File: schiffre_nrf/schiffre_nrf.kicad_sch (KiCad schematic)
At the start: 30 parts, among them J1 Conn_01x02, J2 Conn_01x04, J3 Conn_01x01_Pin, J4 Conn_01x04, J5 FH34SRJ-30S-0.5SH(50), P1 USB_C_Plug_USB2.0, Q1 AO3407, Q2 AO3407, U1 E73-2G4M08S1C, U2 XC6220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

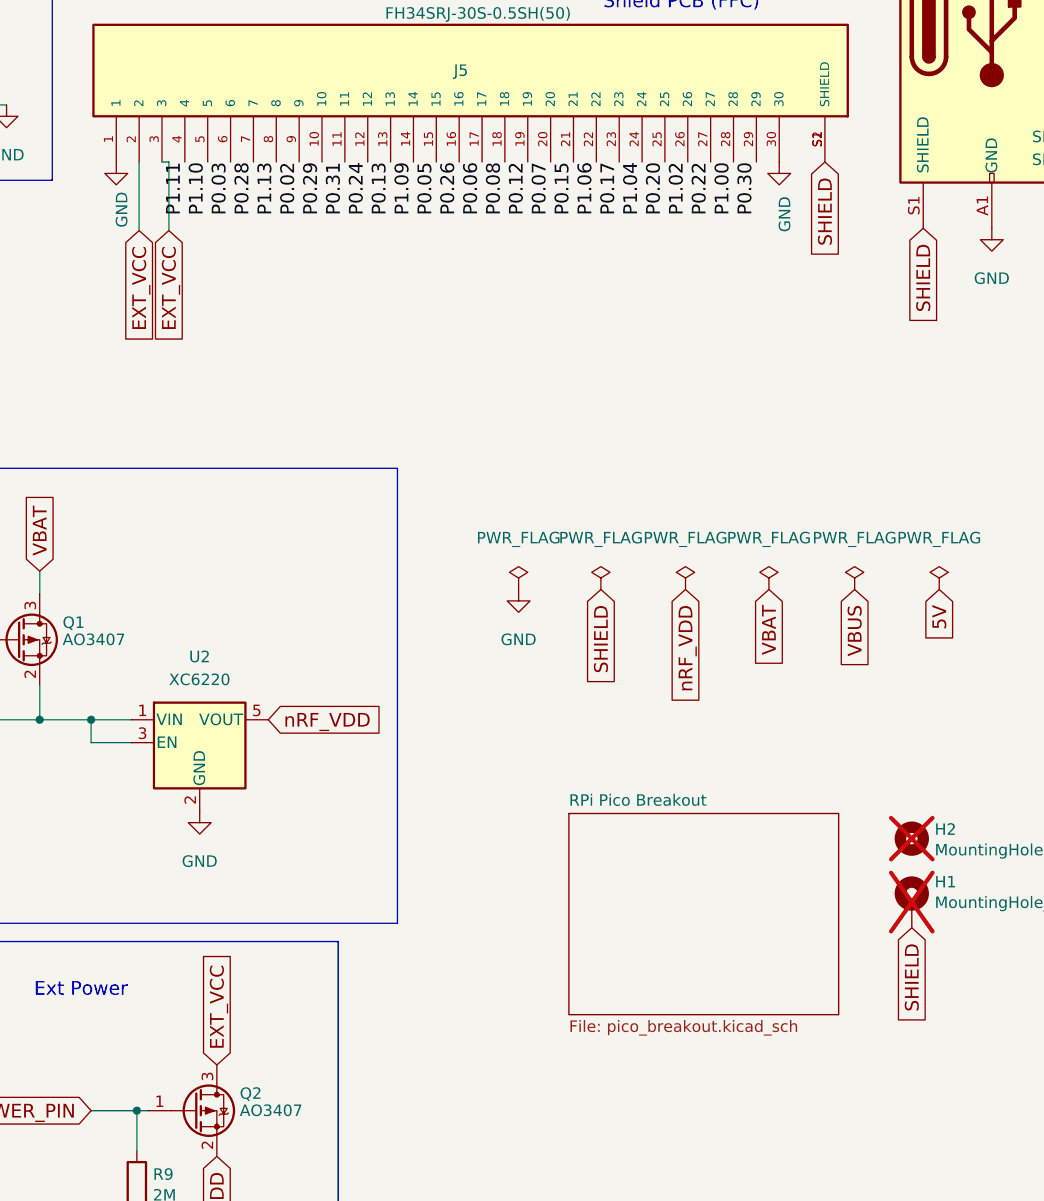
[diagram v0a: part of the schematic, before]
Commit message: factored out the pico breakout board
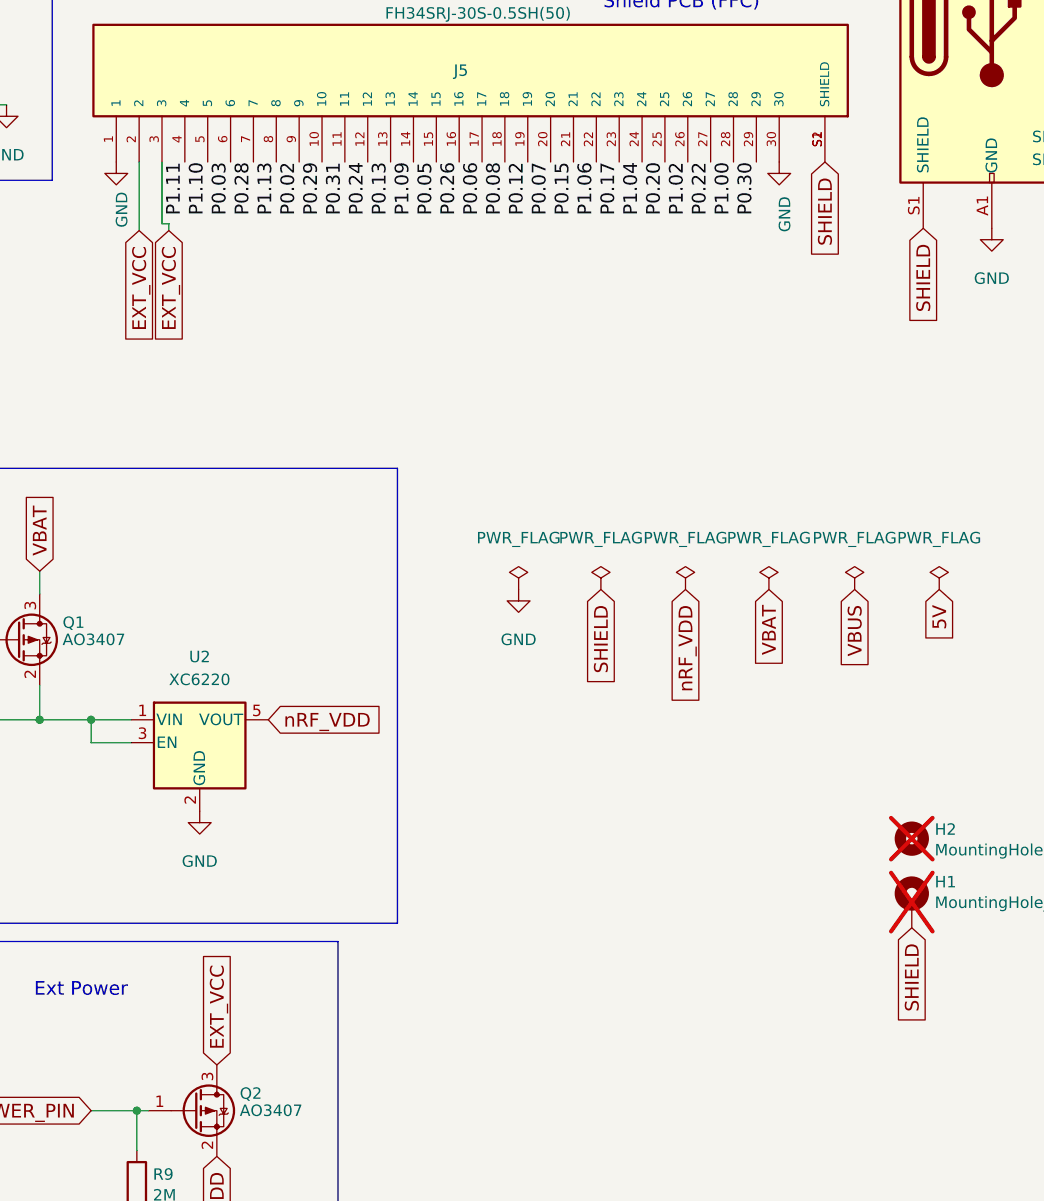
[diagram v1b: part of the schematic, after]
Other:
- removed sheet RPi Pico Breakout
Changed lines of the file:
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@@
+    (stroke (width 0) (type default))
+  )
+  (wire (pts (xy 155.194 71.882) (xy 155.194 65.024))
     (stroke (width 0) (type default))
   )
@@
     (stroke (width 0) (type default))
   )
-  (wire (pts (xy 155.956 65.024) (xy 155.194 65.024))
+  (wire (pts (xy 155.956 71.882) (xy 155.194 71.882))
     (stroke (width 0) (type default))
   )
@@
     (stroke (width 0) (type default))
   )
-  (wire (pts (xy 155.956 72.644) (xy 155.956 65.024))
+  (wire (pts (xy 155.956 72.644) (xy 155.956 71.882))
     (stroke (width 0) (type default))
   )
@@
       )
     )
-  )
-  (sheet (at 200.406 137.414) (size 29.972 22.352) (fields_autoplaced)
-    (stroke (width 0.1524) (type solid))
-    (fill (color 0 0 0 0.0000))
-    (property "Sheetname" "RPi Pico Breakout" (at 200.406 136.7024 0)
-      (effects (font (size 1.27 1.27)) (justify left bottom))
-    )
-    (property "Sheetfile" "pico_breakout.kicad_sch" (at 200.406 160.3506 0)
-      (effects (font (size 1.27 1.27)) (justify left top))
-    )
-    (instances
-      (project "schiffre_nrf"
-        (path "/bfc0aadc-38cf-466e-a642-68fdc3138c78" (page "2"))
-      )
-    )

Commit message: small drc things
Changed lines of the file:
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@@
   (junction (at 147.32 127) (diameter 0) (color 0 0 0 0)
+  )
+  (junction (at 144.018 127) (diameter 0) (color 0 0 0 0)
   )
   (junction (at 58.42 167.64) (diameter 0) (color 0 0 0 0)
@@
     (stroke (width 0) (type default))
   )
-  (wire (pts (xy 141.605 127) (xy 147.32 127))
+  (wire (pts (xy 141.605 127) (xy 144.018 127))
     (stroke (width 0) (type default))
   )
@@
   )
   (wire (pts (xy 76.2 77.47) (xy 93.345 77.47))
+    (stroke (width 0) (type default))
+  )
+  (wire (pts (xy 144.018 127) (xy 147.32 127))
     (stroke (width 0) (type default))
   )
@@
         )
       )
+    )
+  )
+  (symbol (lib_id "power:PWR_FLAG") (at 144.018 127 180) (unit 1)
+    (in_bom yes) (on_board yes) (dnp no) (fields_autoplaced)
+    (property "Reference" "#FLG03" (at 144.018 128.905 0)
+      (effects (font (size 1.27 1.27)) hide)
+    )
+    (property "Value" "PWR_FLAG" (at 144.018 131.826 0)
+      (effects (font (size 1.27 1.27)))
+    )
+    (property "Footprint" "" (at 144.018 127 0)
+      (effects (font (size 1.27 1.27)) hide)
+    )
+    (property "Datasheet" "~" (at 144.018 127 0)
+      (effects (font (size 1.27 1.27)) hide)
+    )
+    (pin "1")
+    (instances
+      (project "schiffre_nrf"
+        (path "/bfc0aadc-38cf-466e-a642-68fdc3138c78"
+          (reference "#FLG03") (unit 1)
+        )
+      )
